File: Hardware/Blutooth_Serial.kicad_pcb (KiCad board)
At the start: 2 copper layers, 60.5 x 48.8 mm, 10 parts, among them J1 Test_Pad, U2 LM2596S-3.3

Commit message: updated schematic
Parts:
- removed REF**: PinHeader_1x06_P2.54mm_Vertical, Connector_PinHeader_2.54mm:PinHeader_1x06_P2.54mm_Vertical
- added J10: Test_Pad, Connector_PinHeader_2.54mm:PinHeader_1x01_P2.54mm_Vertical, F.Cu at (144.5, 82.0)
- added J2: DE9_Receptacle_MountingHoles, Connector_Dsub:DSUB-9_Female_Horizontal_P2.77x2.84mm_EdgePinOffset4.94mm_Housed_MountingHolesOffset7.48mm, F.Cu at (96.7, 90.6)
- added J3: Test_Pad, Connector_PinHeader_2.54mm:PinHeader_1x01_P2.54mm_Vertical, F.Cu at (130.3, 77.4)
- added J4: Test_Pad, Connector_PinHeader_2.54mm:PinHeader_1x01_P2.54mm_Vertical, F.Cu at (130.3, 82.0)
- added J5: Test_Pad, Connector_PinHeader_2.54mm:PinHeader_1x01_P2.54mm_Vertical, F.Cu at (135.0, 77.4)
- added J6: Test_Pad, Connector_PinHeader_2.54mm:PinHeader_1x01_P2.54mm_Vertical, F.Cu at (135.0, 82.0)
- added J7: Test_Pad, Connector_PinHeader_2.54mm:PinHeader_1x01_P2.54mm_Vertical, F.Cu at (139.6, 77.4)
- added J8: Test_Pad, Connector_PinHeader_2.54mm:PinHeader_1x01_P2.54mm_Vertical, F.Cu at (139.6, 82.0)
- added J9: Test_Pad, Connector_PinHeader_2.54mm:PinHeader_1x01_P2.54mm_Vertical, F.Cu at (144.3, 77.4)
- added JP1: SolderJumper_2_Open, Jumper:SolderJumper-2_P1.3mm_Open_Pad1.0x1.5mm, F.Cu at (147.9, 86.1)
- added JP2: SolderJumper_2_Open, Jumper:SolderJumper-2_P1.3mm_Open_Pad1.0x1.5mm, F.Cu at (147.9, 89.7)
- added JP3: SolderJumper_2_Open, Jumper:SolderJumper-2_P1.3mm_Open_Pad1.0x1.5mm, F.Cu at (147.9, 93.2)
- added JP4: SolderJumper_2_Open, Jumper:SolderJumper-2_P1.3mm_Open_Pad1.0x1.5mm, F.Cu at (152.2, 86.1)
- added JP5: SolderJumper_2_Open, Jumper:SolderJumper-2_P1.3mm_Open_Pad1.0x1.5mm, F.Cu at (152.2, 89.7)
- added JP6: SolderJumper_2_Open, Jumper:SolderJumper-2_P1.3mm_Open_Pad1.0x1.5mm, F.Cu at (152.2, 93.2)
- added JP7: SolderJumper_2_Open, Jumper:SolderJumper-2_P1.3mm_Open_Pad1.0x1.5mm, F.Cu at (156.6, 86.1)
- added JP8: SolderJumper_2_Open, Jumper:SolderJumper-2_P1.3mm_Open_Pad1.0x1.5mm, F.Cu at (156.6, 89.7)
- added JP9: SolderJumper_2_Open, Jumper:SolderJumper-2_P1.3mm_Open_Pad1.0x1.5mm, F.Cu at (156.6, 93.2)
- added U3: LM2596S-5, Package_TO_SOT_SMD:TO-263-5_TabPin3, F.Cu at (51.9, 85.3)
- C1: value 150uF -> 470uF
- C2: value 680uF -> 220uF
- L1: value 33uH -> 68uH
- U2: value LM2596S-3.3 -> MAX3232; footprint Package_TO_SOT_SMD:TO-263-5_TabPin3 -> Package_DIP:DIP-16_W8.89mm_SMDSocket_LongPads
- moved J1 81.3 mm to (141.0, 69.3)
- moved U2 22.7 mm to (74.9, 97.3), turned to 0 degrees
- moved VIN+ 17.8 mm to (52.3, 109.5)
- moved D2 16.6 mm to (61.5, 94.2)
- moved IC1 10.6 mm to (87.5, 91.1)
- moved C1 7.46 mm to (52.8, 99.1)
- moved C2 3.14 mm to (55.1, 71.6), turned to 180 degrees
- moved GND 2.96 mm to (47.2, 109.5)
- turned L1 to 0 degrees
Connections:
- C2 pad 1: 3.3V -> 5V
- IC1 pad 2: 3.3V -> Net-(IC1-Vcc)
- IC1 pad 4: unconnected-(IC1-TXD-Pad4) -> T1IN
- IC1 pad 5: unconnected-(IC1-RXD-Pad5) -> R1OUT
- L1 pad 2: 3.3V -> 5V
- U2 pad 1: +24V -> Net-(U2-C1+)
- U2 pad 2: Net-(D2-K) -> Net-(U2-VS+)
- U2 pad 3: GND -> Net-(U2-C1-)
- U2 pad 4: 3.3V -> Net-(U2-C2+)
- U2 pad 5: Net-(J1-Pin_1) -> Net-(U2-C2-)
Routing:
- net GND: track 83.7 -> 0.00 mm, vias 8 -> 0
- net 3.3V: track 74.1 -> 0.00 mm
- net Net-(D2-K): track 18.9 -> 0.00 mm
- net +24V: track 10.5 -> 0.00 mm
- net Net-(J1-Pin_1): track 6.30 -> 0.00 mm
- net unconnected-(IC1-TXD-Pad4): track 4.75 -> 0.00 mm
- net unconnected-(IC1-STATE-Pad6): track 4.75 -> 0.00 mm
- net unconnected-(IC1-RXD-Pad5): track 4.75 -> 0.00 mm
- net unconnected-(IC1-EN-Pad1): track 4.75 -> 0.00 mm
- removed copper zone on F.Cu, net +24V
- removed copper zone on F.Cu, net 3.3V
- removed copper zone on B.Cu, net GND
- removed copper zone on F.Cu, net GND
- removed copper zone on F.Cu, net Net-(D2-K)
- removed copper zone on F.Cu, net Net-(J1-Pin_1)

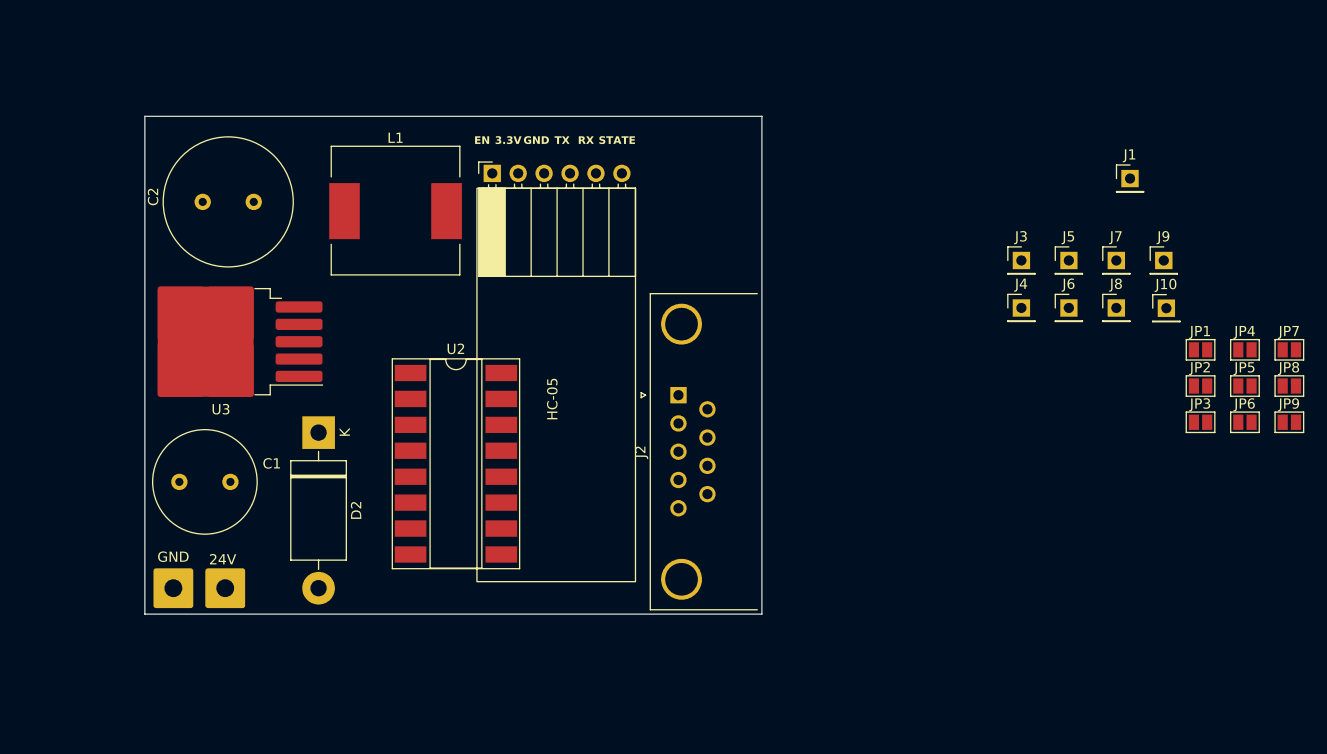
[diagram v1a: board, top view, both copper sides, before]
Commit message: reorganized and switched components
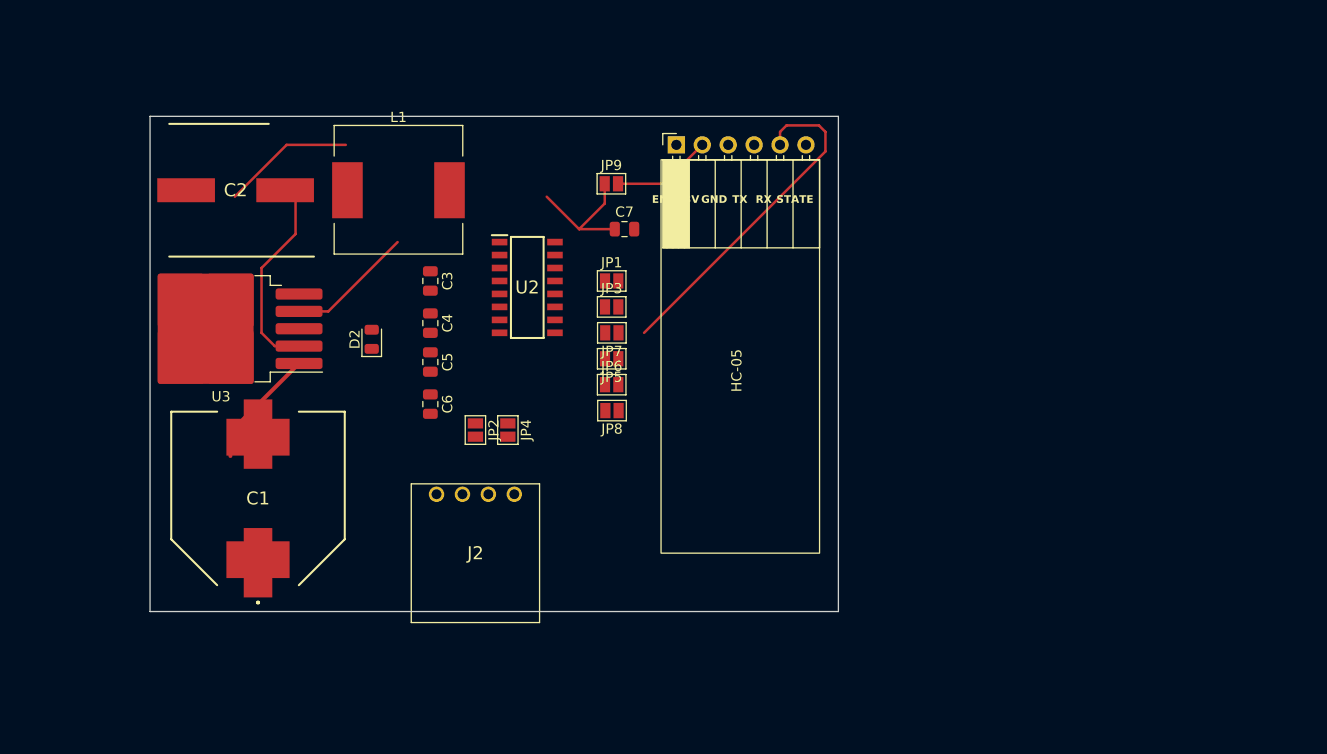
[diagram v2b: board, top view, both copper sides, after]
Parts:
- removed GND: SolderWire-1sqmm_1x01_D1.4mm_OD3.9mm, Connector_Wire:SolderWire-1sqmm_1x01_D1.4mm_OD3.9mm
- removed J1, J10, J3, J4, J5, J6, J7, J8, J9: Test_Pad, Connector_PinHeader_2.54mm:PinHeader_1x01_P2.54mm_Vertical
- removed VIN+: , 
- added C3: 0.1uF, Capacitor_SMD:C_0805_2012Metric, F.Cu at (72.4, 79.4)
- added C4: 0.47uF, Capacitor_SMD:C_0805_2012Metric, F.Cu at (72.4, 83.5)
- added C5: 0.47uF, Capacitor_SMD:C_0805_2012Metric, F.Cu at (72.4, 87.3)
- added C6: 0.47uF, Capacitor_SMD:C_0805_2012Metric, F.Cu at (72.4, 91.4)
- added C7: 0.1uF, Capacitor_SMD:C_0805_2012Metric, F.Cu at (91.4, 74.3)
- C1: footprint Capacitor_THT:C_Radial_D10.0mm_H16.0mm_P5.00mm -> my_lib:470uF_SMD_CAP
- C2: footprint Capacitor_THT:C_Radial_D12.5mm_H25.0mm_P5.00mm -> my_lib:220uF_SMD_CAP
- D2: footprint Diode_THT:D_DO-201AD_P15.24mm_Horizontal -> Diode_SMD:D_0805_2012Metric
- J2: value DE9_Receptacle_MountingHoles -> Conn_01x04_Pin; footprint Connector_Dsub:DSUB-9_Female_Horizontal_P2.77x2.84mm_EdgePinOffset4.94mm_Housed_MountingHolesOffset7.48mm -> my_lib:male_pin_4
- U2: footprint Package_DIP:DIP-16_W8.89mm_SMDSocket_LongPads -> my_lib:MAX3232EIDR
- moved JP4 72.6 mm to (80.0, 94.0), turned to -90 degrees
- moved JP2 71.2 mm to (76.8, 94.0), turned to -90 degrees
- moved JP9 70.4 mm to (90.2, 69.8)
- moved JP8 66.4 mm to (90.2, 92.1), turned to 180 degrees
- moved JP7 66.4 mm to (90.2, 84.5), turned to 180 degrees
- moved JP6 62.2 mm to (90.2, 89.5)
- moved JP5 62.1 mm to (90.2, 87.0), turned to 180 degrees
- moved JP3 58.8 mm to (90.2, 81.9)
- moved JP1 58.1 mm to (90.2, 79.4)
- moved J2 25.2 mm to (76.8, 106.0), turned to 0 degrees
- moved U2 18.6 mm to (81.9, 80.0)
- moved IC1 18.2 mm to (105.5, 88.3)
- moved D2 10.5 mm to (66.7, 85.1), turned to 90 degrees
- moved C1 3.15 mm to (55.5, 100.7), turned to 0 degrees
- moved C2 2.11 mm to (53.3, 70.5)
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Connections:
- net R1IN renamed Net-(J2-Pin_3)
- J2 pad 1: unconnected-(J2-Pad1) -> +24V
- J2 pad 2: T1OUT -> GND
- J2 pad 4: unconnected-(J2-Pad4) -> Net-(J2-Pin_4)
- JP1 pad 2: T1OUT -> Net-(J2-Pin_4)
- JP2 pad 2: T2OUT -> unconnected-(JP2-B-Pad2)
- JP4 pad 2: R2IN -> unconnected-(JP4-B-Pad2)
- JP6 pad 1: T2IN -> unconnected-(JP6-A-Pad1)
- JP8 pad 1: R2OUT -> unconnected-(JP8-A-Pad1)
- U2 pad 16: Net-(U2-VCC) -> 5V
- U3 pad 5: Net-(J1-Pin_1) -> unconnected-(U3-~{ON}/OFF-Pad5)
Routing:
- net 5V: track 0.00 -> 39.4 mm
- net R1OUT: track 0.00 -> 33.3 mm
- net Net-(D2-K): track 0.00 -> 18.9 mm
- net +24V: track 0.00 -> 11.9 mm
- net Net-(IC1-Vcc): track 0.00 -> 9.83 mm
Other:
- board size 60.5 x 48.8 mm -> 67.4 x 48.5 mm
- board text removed: "24V"

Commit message: changes
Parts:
- added G***: LOGO, Library:LOGO, B.Cu at (108.7, 109.0)
- C1: renamed from C2; footprint my_lib:220uF_SMD_CAP -> Library:220uF_SMD_CAP
- C2: renamed from C7; footprint Capacitor_SMD:C_0805_2012Metric -> Library:C_0805_2012Metric
- C3, C4, C5, C6: footprint Capacitor_SMD:C_0805_2012Metric -> Library:C_0805_2012Metric
- C7: renamed from C1; footprint my_lib:470uF_SMD_CAP -> Library:470uF_SMD_CAP
- D1: renamed from D2; footprint Diode_SMD:D_0805_2012Metric -> Library:D_0805_2012Metric
- IC1: footprint my_lib:HC-05 -> Library:HC-05
- J1: renamed from J2; footprint my_lib:male_pin_4 -> Library:male_pin_4
- JP1: renamed from JP9; footprint Jumper:SolderJumper-2_P1.3mm_Open_Pad1.0x1.5mm -> Library:SolderJumper-2_P1.3mm_Open_Pad1.0x1.5mm
- JP2: renamed from JP1; footprint Jumper:SolderJumper-2_P1.3mm_Open_Pad1.0x1.5mm -> Library:SolderJumper-2_P1.3mm_Open_Pad1.0x1.5mm
- JP3, JP5, JP6: footprint Jumper:SolderJumper-2_P1.3mm_Open_Pad1.0x1.5mm -> Library:SolderJumper-2_P1.3mm_Open_Pad1.0x1.5mm
- JP4: renamed from JP7; footprint Jumper:SolderJumper-2_P1.3mm_Open_Pad1.0x1.5mm -> Library:SolderJumper-2_P1.3mm_Open_Pad1.0x1.5mm
- JP7: renamed from JP2; footprint Jumper:SolderJumper-2_P1.3mm_Open_Pad1.0x1.5mm -> Library:SolderJumper-2_P1.3mm_Open_Pad1.0x1.5mm
- JP8: renamed from JP4; footprint Jumper:SolderJumper-2_P1.3mm_Open_Pad1.0x1.5mm -> Library:SolderJumper-2_P1.3mm_Open_Pad1.0x1.5mm
- JP9: renamed from JP8; footprint Jumper:SolderJumper-2_P1.3mm_Open_Pad1.0x1.5mm -> Library:SolderJumper-2_P1.3mm_Open_Pad1.0x1.5mm
- L1: footprint my_lib:L_12x12mm_H6mm -> Library:L_12x12mm_H6mm
- U1: renamed from U3; footprint Package_TO_SOT_SMD:TO-263-5_TabPin3 -> Library:TO-263-5_TabPin3
- U2: footprint my_lib:MAX3232EIDR -> Library:MAX3232EIDR
- moved C2 11.1 mm to (80.6, 76.7), turned to 180 degrees
- moved JP1 6.36 mm to (87.6, 75.7)
- moved U2 5.15 mm to (80.5, 85.0)
- moved JP9 5.13 mm to (87.7, 96.5)
- moved JP6 4.32 mm to (87.7, 93.0)
- moved JP5 3.60 mm to (87.7, 89.6)
- moved C4 3.51 mm to (73.9, 80.3)
- moved JP4 3.02 mm to (87.7, 86.1)
- moved C5 2.89 mm to (73.9, 84.8)
- moved C6 2.73 mm to (73.9, 89.2)
- moved J1 2.69 mm to (78.7, 108.0)
- moved JP3 2.62 mm to (87.7, 82.6)
- moved JP2 2.54 mm to (87.7, 79.1)
- moved C3 2.16 mm to (70.5, 80.3)
- moved D1 1.40 mm to (65.3, 85.1)
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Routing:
- net GND: track 0.00 -> 205.8 mm, vias 0 -> 21
- net Net-(J1-Pin_4): track 0.00 -> 39.0 mm, vias 0 -> 2
- net T1IN: track 0.00 -> 38.8 mm, vias 0 -> 1
- net Net-(J1-Pin_3): track 0.00 -> 32.1 mm, vias 0 -> 2
- net +24V: track 11.9 -> 38.0 mm
- net 5V: track 39.4 -> 59.2 mm
- net Net-(U2-C1+): track 0.00 -> 9.16 mm
- net Net-(JP9-B): track 0.00 -> 8.68 mm
- net Net-(JP6-B): track 0.00 -> 8.29 mm
- net Net-(U2-C1-): track 0.00 -> 8.06 mm
- net Net-(JP7-A): track 0.00 -> 6.43 mm
- net Net-(JP2-A): track 0.00 -> 5.76 mm
- net Net-(JP8-A): track 0.00 -> 5.26 mm
- net R1OUT: track 33.3 -> 28.3 mm
- net Net-(IC1-Vcc): track 9.83 -> 14.8 mm
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- added copper zone on F.Cu, net +24V
- added copper zone on F.Cu, net 5V
- added copper zone on B.Cu, net GND
- added copper zone on F.Cu, net GND
- added copper zone on F.Cu, net Net-(D1-K)
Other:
- board size 67.4 x 48.5 mm -> 68.6 x 49.5 mm
- board text added: "Ver 1.1"
